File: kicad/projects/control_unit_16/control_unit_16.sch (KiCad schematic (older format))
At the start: 54 parts, among them J1 Conn_01x04_Female, J2 Control_signal_backplane, J3 Bus_connection, J4 Aux_connection, J5 Conn_01x16_Female, U1 74HC04, U10 28C256, U11 28C256, U2 28C256, U3 74HC173, U4 74HC377, U5 74HC161, U6 28C256, U7 74HC245, U8 74HC245, U9 74HC138

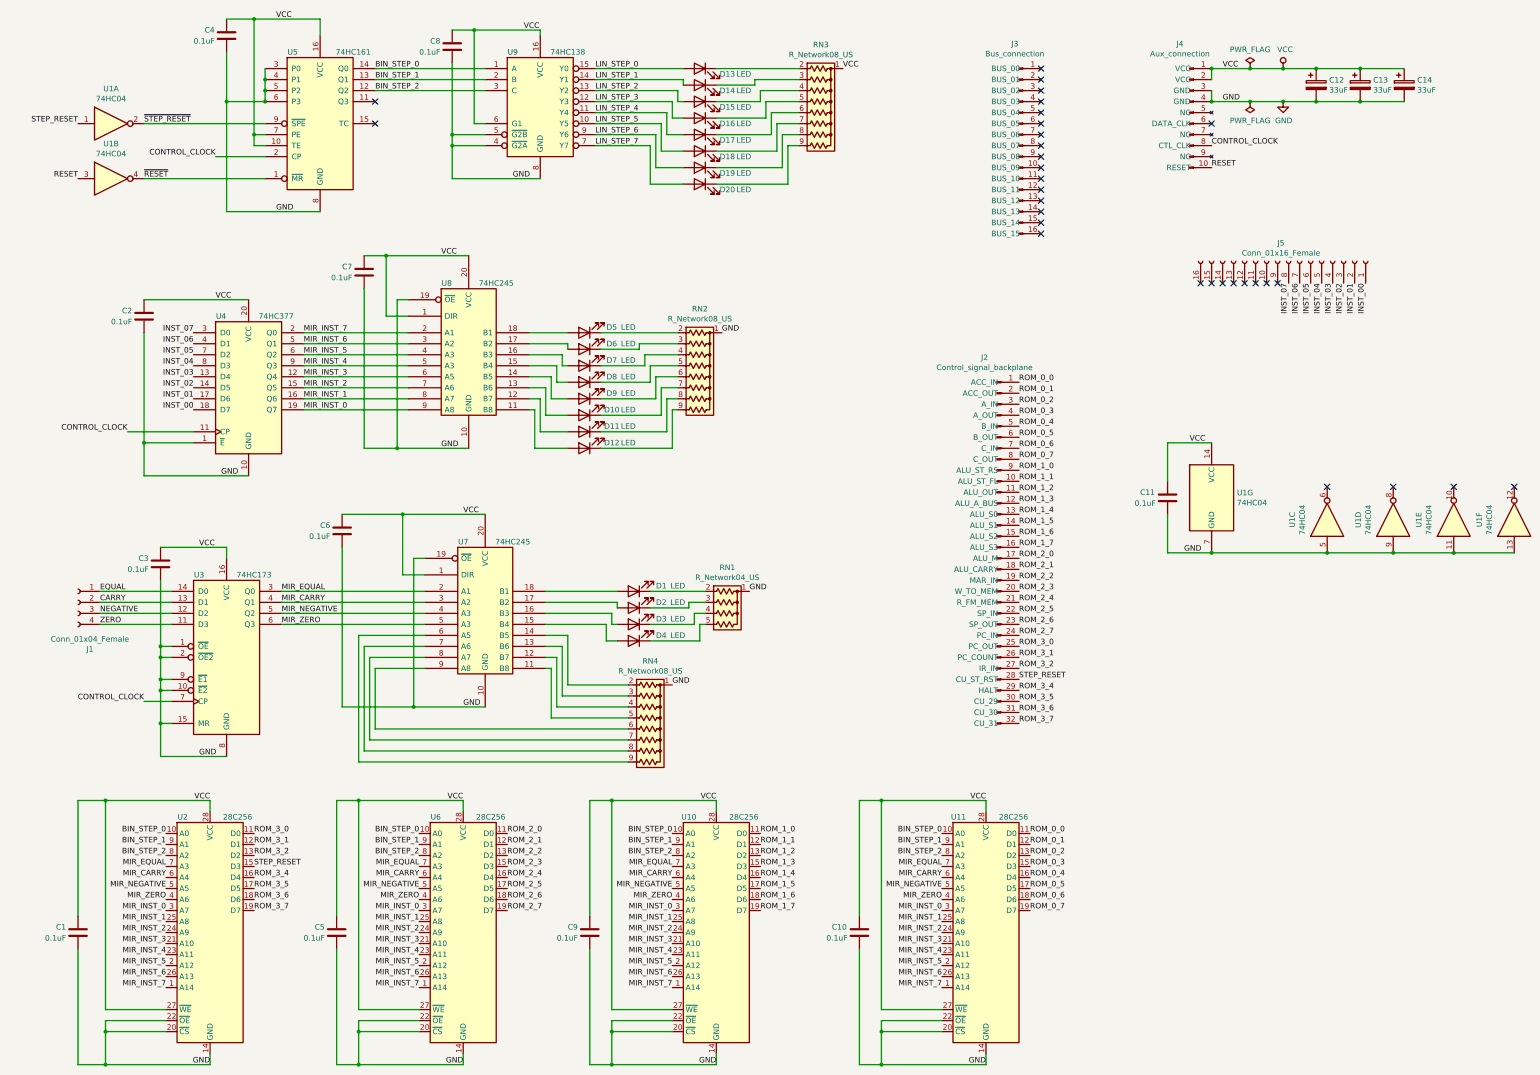
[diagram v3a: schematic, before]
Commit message: Add top power and LED control to control unit.
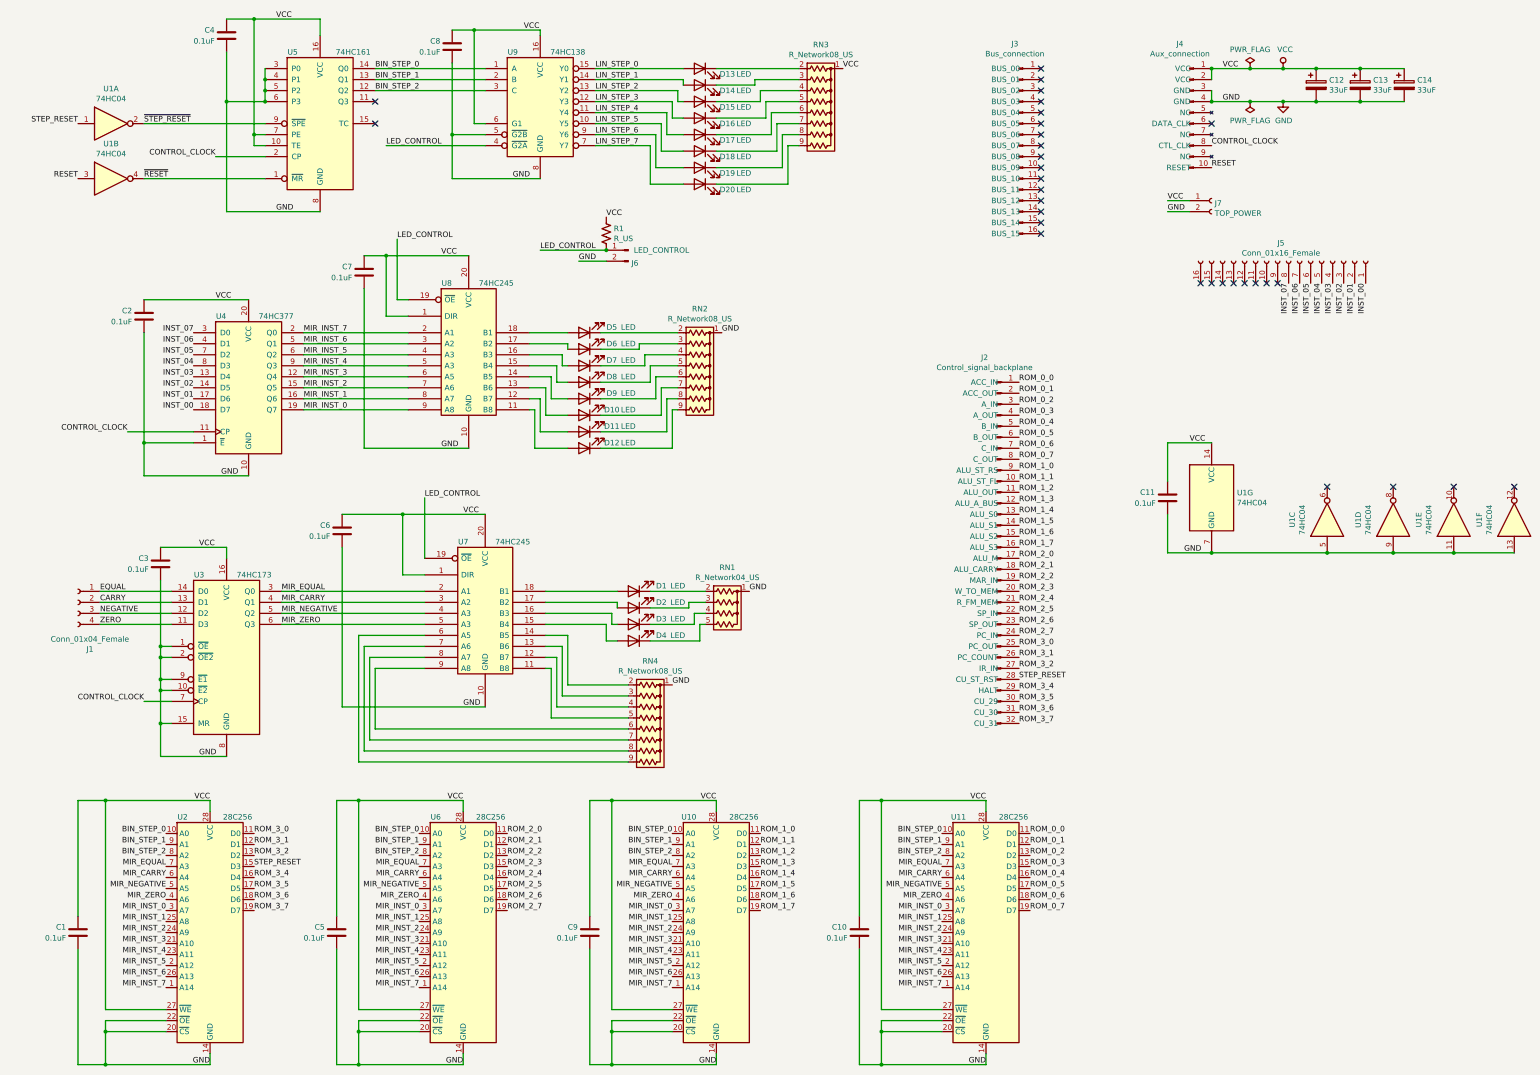
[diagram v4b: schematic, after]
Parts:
- added J6: LED_CONTROL, Connector_PinHeader_2.54mm:PinHeader_1x02_P2.54mm_Horizontal, symbol Connector:Conn_01x02_Male
- added J7: TOP_POWER, Connector_PinSocket_2.54mm:PinSocket_1x02_P2.54mm_Horizontal, symbol Connector:Conn_01x02_Female
- added R1: R_US, Resistor_THT:R_Axial_DIN0207_L6.3mm_D2.5mm_P10.16mm_Horizontal, symbol Device:R_US
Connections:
- net GND: now also J6.2 (Pin_2), J7.2 (Pin_2); no longer U7.19 (~OE), U8.19 (~OE), U9.4 (~G2A)
- net VCC: now also J7.1 (Pin_1), R1.1
- new net LED_CONTROL: J6.1 (Pin_1), R1.2, U7.19 (~OE), U8.19 (~OE), U9.4 (~G2A)
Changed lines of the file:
@@
 Wire Wire Line
 	4450 1700 4450 1050
-Wire Wire Line
-	4750 1800 4450 1800
-Wire Wire Line
-	4450 1800 4450 1700
 Connection ~ 4450 1700
 Wire Wire Line
-	4450 1800 4450 2100
-Wire Wire Line
 	4450 2100 5250 2100
-Connection ~ 4450 1800
 Wire Wire Line
 	4750 1600 4650 1600
@@
 	4050 3350 3850 3350
 Wire Wire Line
-	3650 4550 3950 4550
-Wire Wire Line
-	3950 4550 4600 4550
-Connection ~ 3950 4550
-Wire Wire Line
-	3950 3200 3950 4550
-Wire Wire Line
 	3650 2800 3850 2800
 Wire Wire Line
@@
 $EndComp
 Wire Wire Line
-	4200 5550 4100 5550
-Wire Wire Line
 	4200 5700 4000 5700
-Connection ~ 4100 6900
-Wire Wire Line
-	4100 5550 4100 6900
 Wire Wire Line
 	3450 5150 4000 5150
@@
 Wire Wire Line
 	4200 6150 2900 6150
-Wire Wire Line
-	4100 6900 4750 6900
 Wire Wire Line
 	4200 6550 3750 6550
@@
 	5350 6550 5300 6550
 Wire Wire Line
-	3450 6900 4100 6900
-Wire Wire Line
 	3750 6550 3750 7100
 Wire Wire Line
@@
 	1    0    0    -1
 $EndComp
+$Comp
+L Connector:Conn_01x02_Male J6
+U 1 1 6335DBD4
+P 6050 2750
+F 0 "J6" H 6022 2632 50  0000 R CNN
+F 1 "LED_CONTROL" H 6000 2750 50  0000 R CNN
+F 2 "Connector_PinHeader_2.54mm:PinHeader_1x02_P2.54mm_Horizontal" H 6050 2750 50  0001 C CNN
+F 3 "~" H 6050 2750 50  0001 C CNN
+	1    6050 2750
+	-1   0    0    -1
+$EndComp
+$Comp
+L Connector:Conn_01x02_Female J7
+U 1 1 6335CB5D
+P 11350 2300
+F 0 "J7" H 11378 2276 50  0000 L CNN
+F 1 "TOP_POWER" H 11378 2185 50  0000 L CNN
+F 2 "Connector_PinSocket_2.54mm:PinSocket_1x02_P2.54mm_Horizontal" H 11350 2300 50  0001 C CNN
+F 3 "~" H 11350 2300 50  0001 C CNN
+	1    11350 2300
+	1    0    0    -1
+$EndComp
+Text Label 10950 2300 0    50   ~ 0
+VCC
+Text Label 10950 2400 0    50   ~ 0
+GND
+Text Label 5850 2450 0    50   ~ 0
+VCC
+Text Label 5600 2850 0    50   ~ 0
+GND
+Wire Wire Line
+	10950 2300 11150 2300
+Wire Wire Line
+	10950 2400 11150 2400
+$Comp
+L Device:R_US R1
+U 1 1 633FD3D9
+P 5850 2600
+F 0 "R1" H 5918 2646 50  0000 L CNN
+F 1 "R_US" H 5918 2555 50  0000 L CNN
+F 2 "Resistor_THT:R_Axial_DIN0207_L6.3mm_D2.5mm_P10.16mm_Horizontal" V 5890 2590 50  0001 C CNN
+F 3 "~" H 5850 2600 50  0001 C CNN
+	1    5850 2600
+	1    0    0    -1
+$EndComp
+Text Label 5250 2750 0    50   ~ 0
+LED_CONTROL
+Wire Wire Line
+	5250 2750 5850 2750
+Wire Wire Line
+	5600 2850 5850 2850
+Text Label 4200 5000 0    50   ~ 0
+LED_CONTROL
+Wire Wire Line
+	3450 6900 4750 6900
+Wire Wire Line
+	4200 5550 4200 5000
+Text Label 3950 2650 0    50   ~ 0
+LED_CONTROL
+Wire Wire Line
+	3950 3200 3950 2650
+Wire Wire Line
+	3650 4550 4600 4550
+Text Label 3850 1800 0    50   ~ 0
+LED_CONTROL
+Wire Wire Line
+	4450 1700 4450 2100
+Wire Wire Line
+	3850 1800 4750 1800
+Connection ~ 5850 2750
 $EndSCHEMATC

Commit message: Update LED control and spread traces on Control Unit.
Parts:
- J6: footprint Connector_PinHeader_2.54mm:PinHeader_1x02_P2.54mm_Horizontal -> Connector_PinHeader_2.54mm:PinHeader_1x03_P2.54mm_Horizontal; symbol Connector:Conn_01x02_Male -> Connector:Conn_01x03_Male
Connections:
- net GND: now also J6.3 (Pin_3), R1.1; no longer J6.2 (Pin_2)
- net LED_CONTROL: now also J6.2 (Pin_2); no longer J6.1 (Pin_1)
- net VCC: now also J6.1 (Pin_1); no longer R1.1
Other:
- moved on the sheet: R1
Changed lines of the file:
@@
 $EndComp
 $Comp
-L Connector:Conn_01x02_Male J6
+L Connector:Conn_01x03_Male J6
 U 1 1 6335DBD4
 P 6050 2750
 F 0 "J6" H 6022 2632 50  0000 R CNN
 F 1 "LED_CONTROL" H 6000 2750 50  0000 R CNN
-F 2 "Connector_PinHeader_2.54mm:PinHeader_1x02_P2.54mm_Horizontal" H 6050 2750 50  0001 C CNN
+F 2 "Connector_PinHeader_2.54mm:PinHeader_1x03_P2.54mm_Horizontal" H 6050 2750 50  0001 C CNN
 F 3 "~" H 6050 2750 50  0001 C CNN
 	1    6050 2750
@@
 L Device:R_US R1
 U 1 1 633FD3D9
-P 5850 2600
-F 0 "R1" H 5918 2646 50  0000 L CNN
-F 1 "R_US" H 5918 2555 50  0000 L CNN
-F 2 "Resistor_THT:R_Axial_DIN0207_L6.3mm_D2.5mm_P10.16mm_Horizontal" V 5890 2590 50  0001 C CNN
-F 3 "~" H 5850 2600 50  0001 C CNN
-	1    5850 2600
+P 5600 3000
+F 0 "R1" H 5668 3046 50  0000 L CNN
+F 1 "R_US" H 5668 2955 50  0000 L CNN
+F 2 "Resistor_THT:R_Axial_DIN0207_L6.3mm_D2.5mm_P10.16mm_Horizontal" V 5640 2990 50  0001 C CNN
+F 3 "~" H 5600 3000 50  0001 C CNN
+	1    5600 3000
 	1    0    0    -1
 $EndComp
-Text Label 5250 2750 0    50   ~ 0
+Text Label 5450 2750 2    50   ~ 0
 LED_CONTROL
 Wire Wire Line
-	5250 2750 5850 2750
+	5450 2750 5850 2750
 Wire Wire Line
 	5600 2850 5850 2850
@@
 Wire Wire Line
 	3850 1800 4750 1800
-Connection ~ 5850 2750
+Wire Wire Line
+	5600 3150 5450 3150
+Wire Wire Line
+	5450 3150 5450 2750
+Wire Wire Line
+	5850 2650 5850 2450
 $EndSCHEMATC

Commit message: Couple of fixes to status - tech checks and adding  micro step output to control uint.
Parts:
- J1: footprint Connector_PinSocket_2.54mm:PinSocket_1x04_P2.54mm_Horizontal -> Connector_PinSocket_2.54mm:PinSocket_1x07_P2.54mm_Horizontal; symbol Connector:Conn_01x04_Female -> Connector:Conn_01x07_Female
- R1: value R_US -> 10K
- RN1: value R_Network04_US -> 10K
- RN2, RN4: value R_Network08_US -> 10K
- RN3: value R_Network08_US -> 2K
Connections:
- net BIN_STEP_0: now also J1.1 (Pin_1)
- net BIN_STEP_1: now also J1.2 (Pin_2)
- net BIN_STEP_2: now also J1.3 (Pin_3)
- net CARRY: now also J1.5 (Pin_5); no longer J1.2 (Pin_2)
- net EQUAL: now also J1.4 (Pin_4); no longer J1.1 (Pin_1)
- net NEGATIVE: now also J1.6 (Pin_6); no longer J1.3 (Pin_3)
- net ZERO: now also J1.7 (Pin_7); no longer J1.4 (Pin_4)
- net at U7.11 (B8): now also RN4.6 (R5); no longer RN4.5 (R4)
- net at U7.12 (B7): now also RN4.7 (R6); no longer RN4.4 (R3)
- net at U7.13 (B6): now also RN4.8 (R7); no longer RN4.3 (R2)
- net at U7.14 (B5): now also RN4.9 (R8); no longer RN4.2 (R1)
- net at U7.6 (A5): now also RN4.5 (R4); no longer RN4.9 (R8)
- net at U7.7 (A6): now also RN4.4 (R3); no longer RN4.8 (R7)
- net at U7.8 (A7): now also RN4.3 (R2); no longer RN4.7 (R6)
- net at U7.9 (A8): now also RN4.2 (R1); no longer RN4.6 (R5)
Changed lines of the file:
@@
 P 7800 1500
 F 0 "RN3" V 7183 1500 50  0000 C CNN
-F 1 "R_Network08_US" V 7274 1500 50  0000 C CNN
+F 1 "2K" V 7274 1500 50  0000 C CNN
 F 2 "Resistor_THT:R_Array_SIP9" V 8275 1500 50  0001 C CNN
 F 3 "http://www.vishay.com/docs/31509/csc.pdf" H 7800 1500 50  0001 C CNN
@@
 P 6700 3900
 F 0 "RN2" V 6083 3900 50  0000 C CNN
-F 1 "R_Network08_US" V 6174 3900 50  0000 C CNN
+F 1 "10K" V 6174 3900 50  0000 C CNN
 F 2 "Resistor_THT:R_Array_SIP9" V 7175 3900 50  0001 C CNN
 F 3 "http://www.vishay.com/docs/31509/csc.pdf" H 6700 3900 50  0001 C CNN
@@
 P 6950 6050
 F 0 "RN1" V 6533 6050 50  0000 C CNN
-F 1 "R_Network04_US" V 6624 6050 50  0000 C CNN
+F 1 "10K" V 6624 6050 50  0000 C CNN
 F 2 "Resistor_THT:R_Array_SIP5" V 7225 6050 50  0001 C CNN
 F 3 "http://www.vishay.com/docs/31509/csc.pdf" H 6950 6050 50  0001 C CNN
@@
 $EndComp
 $Comp
-L Connector:Conn_01x04_Female J1
+L Connector:Conn_01x07_Female J1
 U 1 1 5FDB6ECF
-P 1050 5950
-F 0 "J1" H 942 5525 50  0000 C CNN
-F 1 "Conn_01x04_Female" H 942 5616 50  0000 C CNN
-F 2 "Connector_PinSocket_2.54mm:PinSocket_1x04_P2.54mm_Horizontal" H 1050 5950 50  0001 C CNN
-F 3 "~" H 1050 5950 50  0001 C CNN
-	1    1050 5950
+P 800 5850
+F 0 "J1" H 800 5350 50  0000 C CNN
+F 1 "Conn_01x04_Female" H 750 5450 50  0000 C CNN
+F 2 "Connector_PinSocket_2.54mm:PinSocket_1x07_P2.54mm_Horizontal" H 800 5850 50  0001 C CNN
+F 3 "~" H 800 5850 50  0001 C CNN
+	1    800  5850
 	-1   0    0    -1
 $EndComp
@@
 Text Label 8900 9450 2    50   ~ 0
 MIR_INST_7
-Text Label 1250 5850 0    50   ~ 0
+Text Label 1000 5850 0    50   ~ 0
 EQUAL
-Text Label 1250 5950 0    50   ~ 0
+Text Label 1000 5950 0    50   ~ 0
 CARRY
-Text Label 1250 6050 0    50   ~ 0
+Text Label 1000 6050 0    50   ~ 0
 NEGATIVE
-Text Label 1250 6150 0    50   ~ 0
+Text Label 1000 6150 0    50   ~ 0
 ZERO
 Text Label 2900 5850 0    50   ~ 0
@@
 MIR_ZERO
 Wire Wire Line
-	1250 5850 1900 5850
-Wire Wire Line
-	1250 5950 1900 5950
-Wire Wire Line
-	1250 6050 1900 6050
-Wire Wire Line
-	1250 6150 1900 6150
+	1000 5850 1900 5850
+Wire Wire Line
+	1000 5950 1900 5950
+Wire Wire Line
+	1000 6050 1900 6050
+Wire Wire Line
+	1000 6150 1900 6150
 Text Label 9600 6650 0    50   ~ 0
 STEP_RESET
@@
 L Device:R_Network08_US RN4
 U 1 1 60897A38
-P 6250 7100
-F 0 "RN4" V 5633 7100 50  0000 C CNN
-F 1 "R_Network08_US" V 5724 7100 50  0000 C CNN
-F 2 "Resistor_THT:R_Array_SIP9" V 6725 7100 50  0001 C CNN
-F 3 "http://www.vishay.com/docs/31509/csc.pdf" H 6250 7100 50  0001 C CNN
-	1    6250 7100
-	0    1    1    0
+P 6250 7000
+F 0 "RN4" V 5633 7000 50  0000 C CNN
+F 1 "10K" V 5724 7000 50  0000 C CNN
+F 2 "Resistor_THT:R_Array_SIP9" V 6725 7000 50  0001 C CNN
+F 3 "http://www.vishay.com/docs/31509/csc.pdf" H 6250 7000 50  0001 C CNN
+	1    6250 7000
+	0    1    -1   0
 $EndComp
 $Comp
@@
 	3750 6550 3750 7100
 Wire Wire Line
-	3750 7100 6050 7100
-Wire Wire Line
-	6050 7200 3700 7200
-Wire Wire Line
 	3700 7200 3700 6450
 Wire Wire Line
@@
 	3650 6350 3650 7300
 Wire Wire Line
-	3650 7300 6050 7300
-Wire Wire Line
 	3650 6350 4200 6350
 Wire Wire Line
-	6050 7400 3600 7400
-Wire Wire Line
 	3600 7400 3600 6250
 Wire Wire Line
 	3600 6250 4200 6250
-Text Label 6450 6700 0    50   ~ 0
+Text Label 6450 7400 0    50   ~ 0
 GND
 Text Label 2350 4800 0    50   ~ 0
@@
 P 5600 3000
 F 0 "R1" H 5668 3046 50  0000 L CNN
-F 1 "R_US" H 5668 2955 50  0000 L CNN
+F 1 "10K" H 5668 2955 50  0000 L CNN
 F 2 "Resistor_THT:R_Axial_DIN0207_L6.3mm_D2.5mm_P10.16mm_Horizontal" V 5640 2990 50  0001 C CNN
-F 3 "~" H 5600 3000 50  0001 C CNN
+F 3 "" H 5600 3000 50  0001 C CNN
 	1    5600 3000
 	1    0    0    -1
@@
 Wire Wire Line
 	5850 2650 5850 2450
+Text Label 1000 5550 0    50   ~ 0
+BIN_STEP_0
+Text Label 1000 5650 0    50   ~ 0
+BIN_STEP_1
+Text Label 1000 5750 0    50   ~ 0
+BIN_STEP_2
+Wire Wire Line
+	3750 7100 5350 7100
+Wire Wire Line
+	5350 7100 5350 7400
+Wire Wire Line
+	5350 7400 6050 7400
+Wire Wire Line
+	3700 7200 5300 7200
+Wire Wire Line
+	5300 7200 5300 7300
+Wire Wire Line
+	5300 7300 6050 7300
+Wire Wire Line
+	3650 7300 5250 7300
+Wire Wire Line
+	5250 7300 5250 7250
+Wire Wire Line
+	5250 7250 5400 7250
+Wire Wire Line
+	5400 7250 5400 7200
+Wire Wire Line
+	5400 7200 6050 7200
+Wire Wire Line
+	3600 7400 5200 7400
+Wire Wire Line
+	5200 7400 5200 7150
+Wire Wire Line
+	5200 7150 5400 7150
+Wire Wire Line
+	5400 7150 5400 7100
+Wire Wire Line
+	5400 7100 6050 7100
 $EndSCHEMATC

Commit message: Part way through generating gerbers. Updated control unit chips to be sockets.
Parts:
- U1: footprint Package_DIP:DIP-14_W7.62mm -> Package_DIP:DIP-14_W7.62mm_Socket
- U3, U5, U9: footprint Package_DIP:DIP-16_W7.62mm -> Package_DIP:DIP-16_W7.62mm_Socket
- U4, U7, U8: footprint Package_DIP:DIP-20_W7.62mm -> Package_DIP:DIP-20_W7.62mm_Socket
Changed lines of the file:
@@
 F 0 "U5" H 3000 2250 50  0000 C CNN
 F 1 "74HC161" H 3550 2250 50  0000 C CNN
-F 2 "Package_DIP:DIP-16_W7.62mm" H 3250 1600 50  0001 C CNN
+F 2 "Package_DIP:DIP-16_W7.62mm_Socket" H 3250 1600 50  0001 C CNN
 F 3 "https://www.ti.com/lit/ds/symlink/cd54hc163.pdf" H 3250 1600 50  0001 C CNN
 	1    3250 1600
@@
 F 0 "U9" H 5000 1850 50  0000 C CNN
 F 1 "74HC138" H 5500 1850 50  0000 C CNN
-F 2 "Package_DIP:DIP-16_W7.62mm" H 5250 1400 50  0001 C CNN
+F 2 "Package_DIP:DIP-16_W7.62mm_Socket" H 5250 1400 50  0001 C CNN
 F 3 "https://www.ti.com/lit/ds/symlink/sn74hct138.pdf" H 5250 1400 50  0001 C CNN
 	1    5250 1400
@@
 F 0 "U3" H 2150 7200 50  0000 C CNN
 F 1 "74HC173" H 2650 7200 50  0000 C CNN
-F 2 "Package_DIP:DIP-16_W7.62mm" H 2400 6450 50  0001 C CNN
+F 2 "Package_DIP:DIP-16_W7.62mm_Socket" H 2400 6450 50  0001 C CNN
 F 3 "http://www.ti.com/lit/ds/symlink/cd74hc173.pdf" H 2400 6450 50  0001 C CNN
 	1    2400 6450
@@
 F 0 "U1" H 1350 1917 50  0000 C CNN
 F 1 "74HC04" H 1350 1826 50  0000 C CNN
-F 2 "Package_DIP:DIP-14_W7.62mm" H 1350 1600 50  0001 C CNN
+F 2 "Package_DIP:DIP-14_W7.62mm_Socket" H 1350 1600 50  0001 C CNN
 F 3 "https://assets.nexperia.com/documents/data-sheet/74HC_HCT04.pdf" H 1350 1600 50  0001 C CNN
 	1    1350 1600
@@
 F 0 "U1" H 1350 2417 50  0000 C CNN
 F 1 "74HC04" H 1350 2326 50  0000 C CNN
-F 2 "Package_DIP:DIP-14_W7.62mm" H 1350 2100 50  0001 C CNN
+F 2 "Package_DIP:DIP-14_W7.62mm_Socket" H 1350 2100 50  0001 C CNN
 F 3 "https://assets.nexperia.com/documents/data-sheet/74HC_HCT04.pdf" H 1350 2100 50  0001 C CNN
 	2    1350 2100
@@
 F 0 "U1" H 12400 5517 50  0000 C CNN
 F 1 "74HC04" H 12400 5426 50  0000 C CNN
-F 2 "Package_DIP:DIP-14_W7.62mm" H 12400 5200 50  0001 C CNN
+F 2 "Package_DIP:DIP-14_W7.62mm_Socket" H 12400 5200 50  0001 C CNN
 F 3 "https://assets.nexperia.com/documents/data-sheet/74HC_HCT04.pdf" H 12400 5200 50  0001 C CNN
 	3    12400 5200
@@
 F 0 "U1" H 13000 5517 50  0000 C CNN
 F 1 "74HC04" H 13000 5426 50  0000 C CNN
-F 2 "Package_DIP:DIP-14_W7.62mm" H 13000 5200 50  0001 C CNN
+F 2 "Package_DIP:DIP-14_W7.62mm_Socket" H 13000 5200 50  0001 C CNN
 F 3 "https://assets.nexperia.com/documents/data-sheet/74HC_HCT04.pdf" H 13000 5200 50  0001 C CNN
 	4    13000 5200
@@
 F 0 "U1" H 13550 5517 50  0000 C CNN
 F 1 "74HC04" H 13550 5426 50  0000 C CNN
-F 2 "Package_DIP:DIP-14_W7.62mm" H 13550 5200 50  0001 C CNN
+F 2 "Package_DIP:DIP-14_W7.62mm_Socket" H 13550 5200 50  0001 C CNN
 F 3 "https://assets.nexperia.com/documents/data-sheet/74HC_HCT04.pdf" H 13550 5200 50  0001 C CNN
 	5    13550 5200
@@
 F 0 "U1" H 14100 5517 50  0000 C CNN
 F 1 "74HC04" H 14100 5426 50  0000 C CNN
-F 2 "Package_DIP:DIP-14_W7.62mm" H 14100 5200 50  0001 C CNN
+F 2 "Package_DIP:DIP-14_W7.62mm_Socket" H 14100 5200 50  0001 C CNN
 F 3 "https://assets.nexperia.com/documents/data-sheet/74HC_HCT04.pdf" H 14100 5200 50  0001 C CNN
 	6    14100 5200
@@
 F 0 "U1" H 11580 5046 50  0000 L CNN
 F 1 "74HC04" H 11580 4955 50  0000 L CNN
-F 2 "Package_DIP:DIP-14_W7.62mm" H 11350 5000 50  0001 C CNN
+F 2 "Package_DIP:DIP-14_W7.62mm_Socket" H 11350 5000 50  0001 C CNN
 F 3 "https://assets.nexperia.com/documents/data-sheet/74HC_HCT04.pdf" H 11350 5000 50  0001 C CNN
 	7    11350 5000
@@
 F 0 "U8" H 4400 4450 50  0000 C CNN
 F 1 "74HC245" H 4850 4450 50  0000 C CNN
-F 2 "Package_DIP:DIP-20_W7.62mm" H 4250 3750 50  0001 C CNN
+F 2 "Package_DIP:DIP-20_W7.62mm_Socket" H 4250 3750 50  0001 C CNN
 F 3 "" H 4250 3750 50  0001 C CNN
 	1    4600 3750
@@
 F 0 "U7" H 4550 6800 50  0000 C CNN
 F 1 "74HC245" H 5000 6800 50  0000 C CNN
-F 2 "Package_DIP:DIP-20_W7.62mm" H 4400 6100 50  0001 C CNN
+F 2 "Package_DIP:DIP-20_W7.62mm_Socket" H 4400 6100 50  0001 C CNN
 F 3 "" H 4400 6100 50  0001 C CNN
 	1    4750 6100
@@
 F 0 "U4" H 2350 4650 50  0000 C CNN
 F 1 "74HC377" H 2850 4650 50  0000 C CNN
-F 2 "Package_DIP:DIP-20_W7.62mm" H 2600 4000 50  0001 C CNN
+F 2 "Package_DIP:DIP-20_W7.62mm_Socket" H 2600 4000 50  0001 C CNN
 F 3 "http://www.ti.com/lit/gpn/sn74LS377" H 2600 4000 50  0001 C CNN
 	1    2600 4000
